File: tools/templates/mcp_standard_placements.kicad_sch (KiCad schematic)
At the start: 150 parts, among them J1 ICSP, J3 PIR BOARD, J5 MOTOR, J6 DNP, Q1 FMOS3401A?, Q11 MMBTA55?, Q2 BC847B?, Q3 MMBTA55?, Q4 MMBTA55?, Q5 MMBTA55?, Q6 MMBTA55?, Q7 BC857C?, Q8 N/P pair? (372A), Q9 DNP, U1 S-1200B45? [pins], U106 U6A / DNP, U2 SN74LVC2G14DBV?, U3 SGM8542XS, U4 PIC16F18855, U5 MX512H, U6 S-812C33AMC? / 3.3V, U7 DNP, Y1 20 MHz

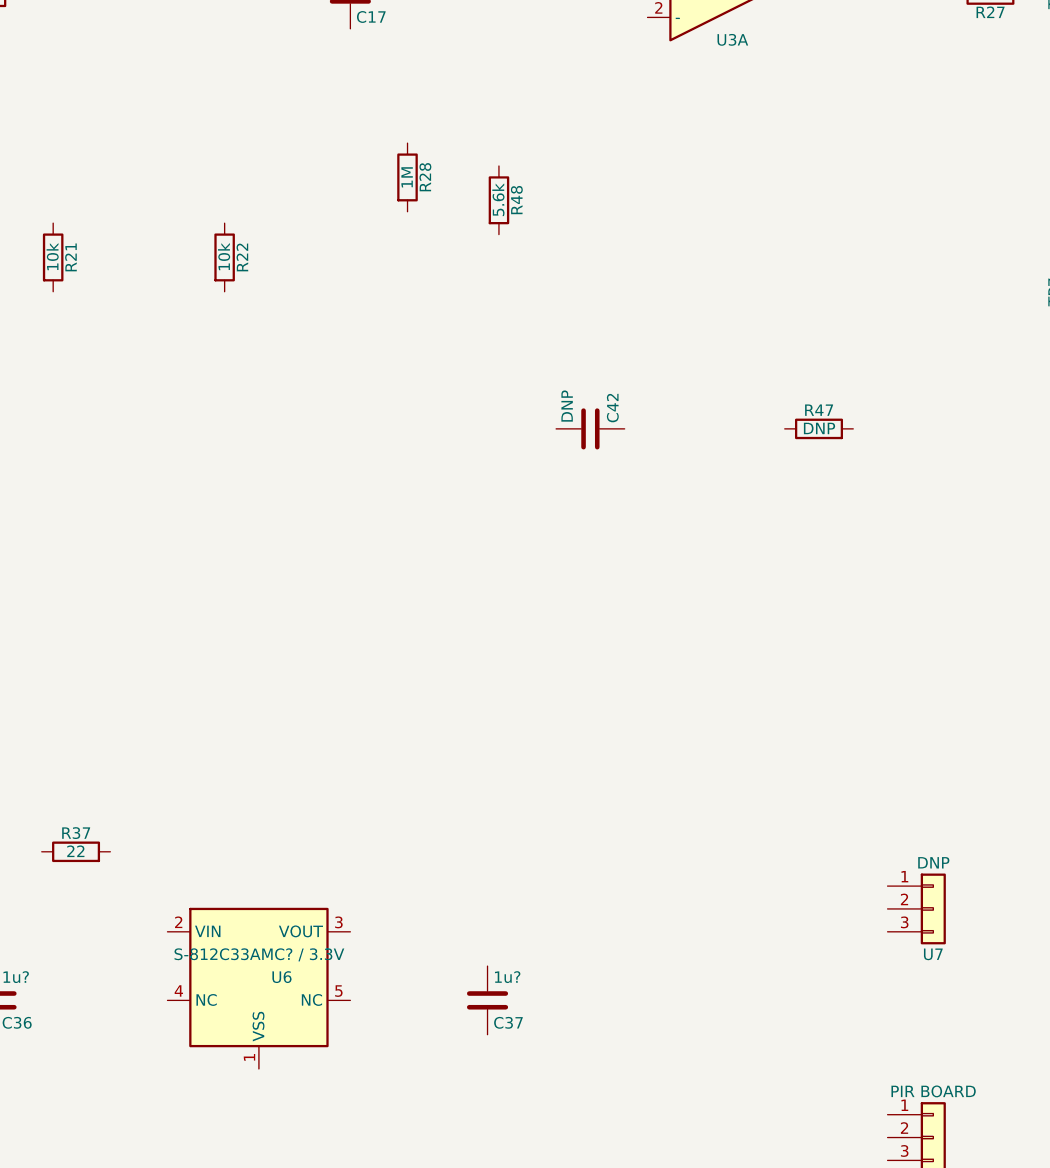
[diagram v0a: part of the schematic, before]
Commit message: Resolve receiver option wiring and measured D6 U6 connections
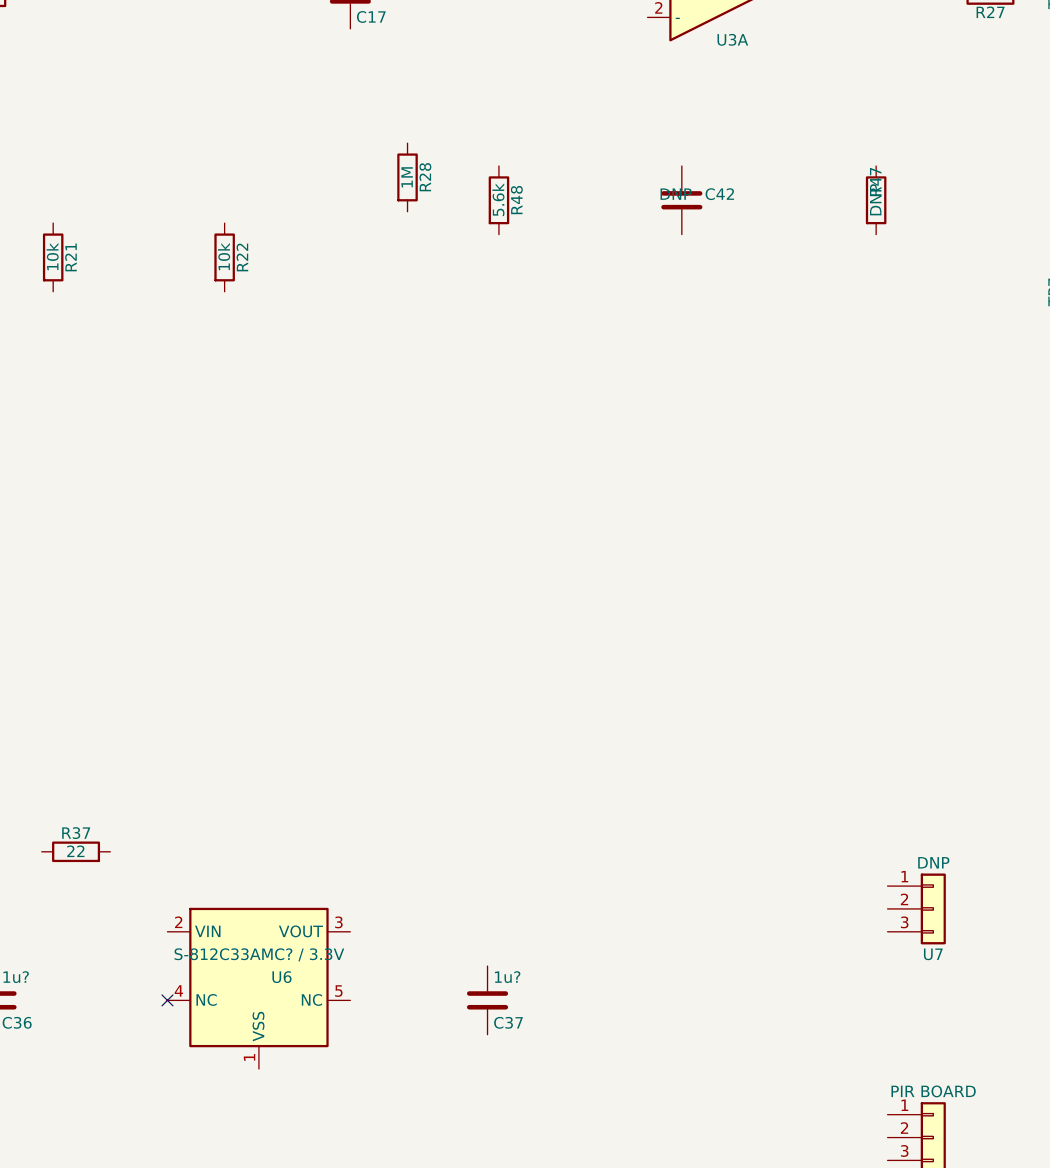
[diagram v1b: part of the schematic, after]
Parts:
- C42, R25, R47, R48: ConnectionEvidence (none) -> v0.9.19 user annotated local copper: R47 left -> U3.1/R27 r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
- D6: ConnectionEvidence (none) -> v0.9.20 B22-B27: upper photo contact V -> GND, lower W -> V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
- U6: ConnectionEvidence (none) -> v0.9.20: U6.5-U6.2 measured 1 ohm (B28). User annotation al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
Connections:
- no-connect marks 0 -> 1
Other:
- moved on the sheet: C42, R47
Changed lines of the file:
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@@
 			)
 		)
-    (property "ConnectionEvidence" "v0.9.18: C6 is reconstructed in parallel with C5 from the user proposal and photos IMG_2431/IMG_2432. C6 upper pad/model1 joins the C5-positive supply copper (H_RF_VDD, after L1); lower pad/model2 joins GND. Photo-supported, not a new meter-confirmed connection. C6 capacitance remains unknown. Earlier 400 kohm output exclusion and 10 ohm Q8-supply-path reading are retained; the latter does not independently prove Q8 source wiring." (at 237.49 181.61 0)
-      (effects (font (size 1.27 1.27)) (hide yes))
-    )
+		(property "ConnectionEvidence" "v0.9.18: C6 is reconstructed in parallel with C5 from the user proposal and photos IMG_2431/IMG_2432. C6 upper pad/model1 joins the C5-positive supply copper (H_RF_VDD, after L1); lower pad/model2 joins GND. Photo-supported, not a new meter-confirmed connection. C6 capacitance remains unknown. Earlier 400 kohm output exclusion and 10 ohm Q8-supply-path reading are retained; the latter does not independently prove Q8 source wiring."
+			(at 237.49 181.61 0)
+			(effects
+				(font
+					(size 1.27 1.27)
+				)
+				(hide yes)
+			)
+		)
 		(pin "1"
 		)
@@
 			)
 		)
-    (property "ConnectionEvidence" "v0.9.18: C6 is reconstructed in parallel with C5 from the user proposal and photos IMG_2431/IMG_2432. C6 upper pad/model1 joins the C5-positive supply copper (H_RF_VDD, after L1); lower pad/model2 joins GND. Photo-supported, not a new meter-confirmed connection. C6 capacitance remains unknown. Earlier 400 kohm output exclusion and 10 ohm Q8-supply-path reading are retained; the latter does not independently prove Q8 source wiring." (at 259.08 181.61 0)
-      (effects (font (size 1.27 1.27)) (hide yes))
-    )
+		(property "ConnectionEvidence" "v0.9.18: C6 is reconstructed in parallel with C5 from the user proposal and photos IMG_2431/IMG_2432. C6 upper pad/model1 joins the C5-positive supply copper (H_RF_VDD, after L1); lower pad/model2 joins GND. Photo-supported, not a new meter-confirmed connection. C6 capacitance remains unknown. Earlier 400 kohm output exclusion and 10 ohm Q8-supply-path reading are retained; the latter does not independently prove Q8 source wiring."
+			(at 259.08 181.61 0)
+			(effects
+				(font
+					(size 1.27 1.27)
+				)
+				(hide yes)
+			)
+		)
 		(pin "1"
 		)
@@
 			)
 		)
+		(property "ConnectionEvidence" "v0.9.19 user annotated local copper: R47 left -> U3.1/R27 right; R47 right + C42 lower + R25 lower + R48 right share RX_STAGE_LINK. C42 upper -> GND inferred from continuous copper beside U3.4 in IMG_2429/2434. R25-GND and R48-VREF old assumptions withdrawn. R47/C42 remain DNP. No meter reading supplied."
+			(at 356.87 223.52 0)
+			(effects
+				(font
+					(size 1.27 1.27)
+				)
+				(hide yes)
+			)
+		)
 		(pin "1"
 		)
@@
 			)
 		)
+		(property "ConnectionEvidence" "v0.9.19 user annotated local copper: R47 left -> U3.1/R27 right; R47 right + C42 lower + R25 lower + R48 right share RX_STAGE_LINK. C42 upper -> GND inferred from continuous copper beside U3.4 in IMG_2429/2434. R25-GND and R48-VREF old assumptions withdrawn. R47/C42 remain DNP. No meter reading supplied."
+			(at 527.05 215.9 0)
+			(effects
+				(font
+					(size 1.27 1.27)
+				)
+				(hide yes)
+			)
+		)
 		(pin "1"
 		)
@@
 	(symbol
 		(lib_id "Device:C")
-		(at 367.03 248.92 90)
+		(at 377.19 223.52 0)
 		(unit 1)
 		(body_style 1)
@@
 		(dnp no)
 		(property "Reference" "C42"
-			(at 369.57 248.285 0)
+			(at 379.73 222.88500000000002 0)
 			(show_name no)
 			(do_not_autoplace no)
@@
 		)
 		(property "Value" "DNP"
-			(at 364.49 248.285 0)
+			(at 374.65000000000003 222.88500000000002 0)
 			(show_name no)
 			(do_not_autoplace no)
@@
 		)
 		(property "Footprint" "Capacitor_SMD:C_0603_1608Metric"
-			(at 363.22 247.955 0)
+			(at 373.38000000000005 222.55500000000004 0)
 			(hide yes)
 			(show_name no)
@@
 		)
 		(property "Datasheet" ""
-			(at 367.03 248.92 0)
+			(at 377.19 223.52 0)
 			(hide yes)
 			(show_name no)
@@
 		)
 		(property "Description" "Unpolarized capacitor"
-			(at 367.03 248.92 0)
+			(at 377.19 223.52 0)
 			(hide yes)
 			(show_name no)
@@
 			)
 		)
+		(property "ConnectionEvidence" "v0.9.19 user annotated local copper: R47 left -> U3.1/R27 right; R47 right + C42 lower + R25 lower + R48 right share RX_STAGE_LINK. C42 upper -> GND inferred from continuous copper beside U3.4 in IMG_2429/2434. R25-GND and R48-VREF old assumptions withdrawn. R47/C42 remain DNP. No meter reading supplied."
+			(at 377.19 223.52 0)
+			(effects
+				(font
+					(size 1.27 1.27)
+				)
+				(hide yes)
+			)
+		)
 		(pin "1"
 		)
@@
 	(symbol
 		(lib_id "Device:R")
-		(at 392.43 248.92 90)
+		(at 398.78 223.52 0)
 		(unit 1)
 		(body_style 1)
@@
 		(dnp no)
 		(property "Reference" "R47"
-			(at 392.43 246.888 90)
+			(at 398.78 221.48800000000003 90)
 			(show_name no)
 			(do_not_autoplace no)
@@
 		)
 		(property "Value" "DNP"
-			(at 392.43 248.92 90)
+			(at 398.78 223.52 90)
 			(show_name no)
 			(do_not_autoplace no)
@@
 		)
 		(property "Footprint" "Resistor_SMD:R_0603_1608Metric"
-			(at 392.43 250.698 90)
+			(at 398.78 225.29800000000003 90)
 			(hide yes)
 			(show_name no)
@@
 		)
 		(property "Datasheet" ""
-			(at 392.43 248.92 0)
+			(at 398.78 223.52 0)
 			(hide yes)
 			(show_name no)
@@
 		)
 		(property "Description" "Resistor"
-			(at 392.43 248.92 0)
+			(at 398.78 223.52 0)
 			(hide yes)
 			(show_name no)
@@
 			)
 		)
+		(property "ConnectionEvidence" "v0.9.19 user annotated local copper: R47 left -> U3.1/R27 right; R47 right + C42 lower + R25 lower + R48 right share RX_STAGE_LINK. C42 upper -> GND inferred from continuous copper beside U3.4 in IMG_2429/2434. R25-GND and R48-VREF old assumptions withdrawn. R47/C42 remain DNP. No meter reading supplied."
+			(at 398.78 223.52 0)
+			(effects
+				(font
+					(size 1.27 1.27)
+				)
+				(hide yes)
+			)
+		)
 		(pin "1"
 		)
@@
 		)
 	)
+	(no_connect
+		(at 320.03999999999996 312.42)
+	)
 	(sheet_instances
 		(path "/"
@@
 			)
 		)
+		(property "ConnectionEvidence" "v0.9.20: U6.5-U6.2 measured 1 ohm (B28). User annotation also joins physical L2/native5 to R37 upper/model2 and empty U6A single/native1. U6.4/L1 marked NC by user and appears as an isolated surface stub in original photos. Candidate pin5 is internally NC but externally tied to VIN; pin4 remains unused."
+			(at 330.2 309.88 0)
+			(effects
+				(font
+					(size 1.27 1.27)
+				)
+				(hide yes)
+			)
+		)
 		(pin "1"
 		)
@@
 			)
 		)
+    (property "ConnectionEvidence" "v0.9.20 B22-B27: upper photo contact V -> GND, lower W -> VPP, each 1 ohm. B29 red V/black W about 0.7V; B30 reverse OL. Supports A=V/GND (pin2), K=W/VPP (pin1). G3 identity and Zener breakdown remain unverified; no 3.9V measurement." (at 405.13 391.16 0)
+      (effects (font (size 1.27 1.27)) (hide yes))
+    )
 		(pin "1"
 		)

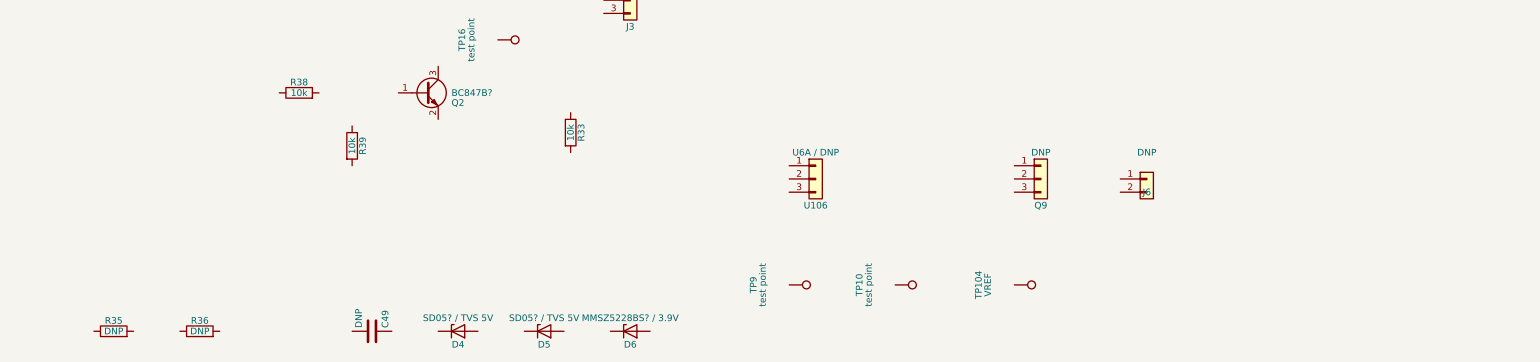
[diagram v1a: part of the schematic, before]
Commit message: Map J6 Q9 option and correct button routing to VPP
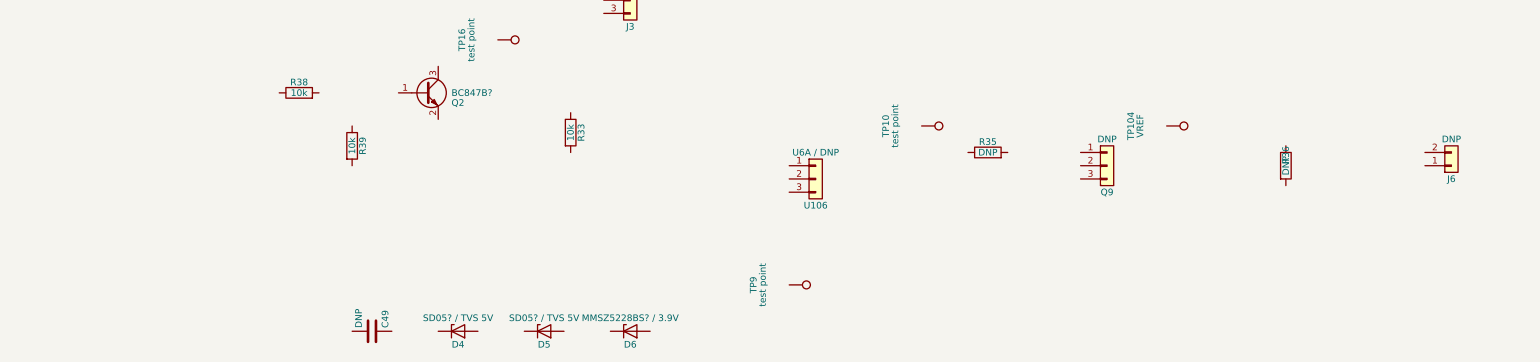
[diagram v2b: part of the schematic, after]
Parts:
- C35, R40, R41, S1: ConnectionEvidence (none) -> v0.9.21 user annotated S1 upper-right to C35 upper/model2 (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
- J6, Q9, R35, R36, TP10: ConnectionEvidence (none) -> v0.9.21 annotated photo: J6 left/model1 joins Q9 single/nat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
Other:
- moved on the sheet: J6, Q9, R35, R36, TP10, TP104

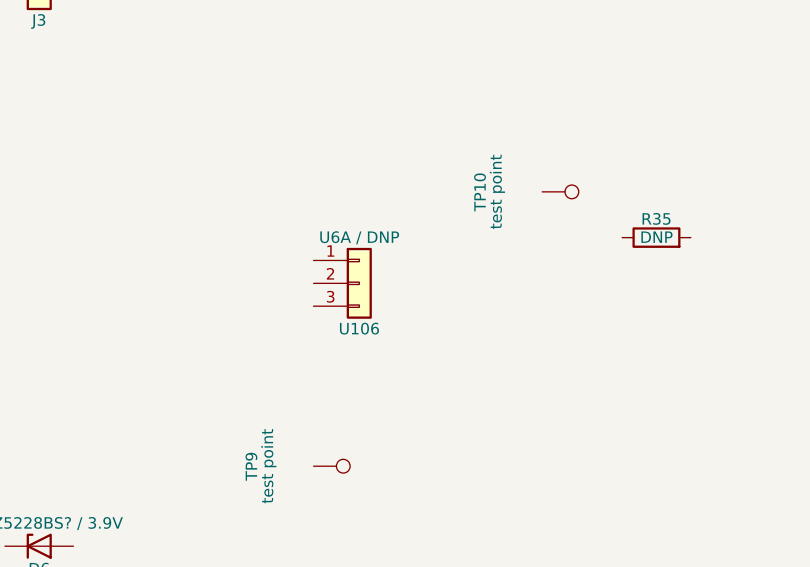
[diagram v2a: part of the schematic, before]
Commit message: Complete U6A option pad mapping with confirmed ground
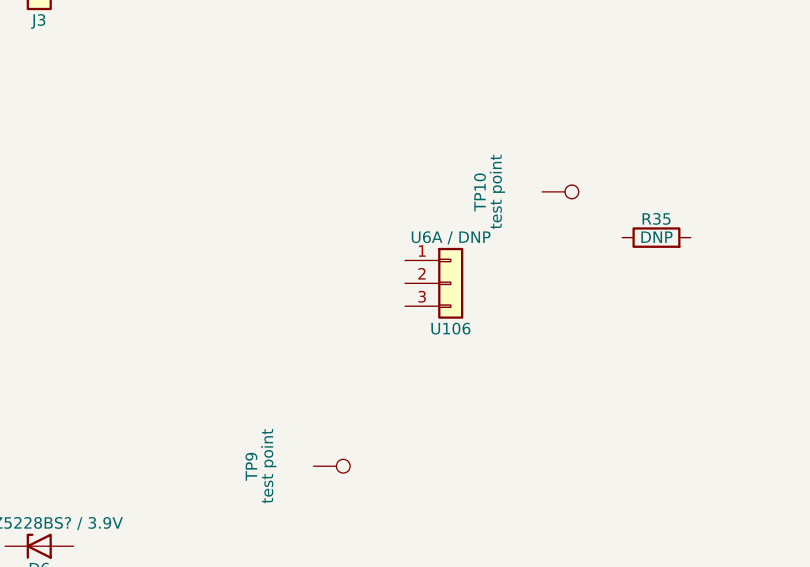
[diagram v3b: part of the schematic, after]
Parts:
- U106: ConnectionEvidence (none) -> v0.9.22 user annotated U6A option: single left pad/model L/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
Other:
- moved on the sheet: U106
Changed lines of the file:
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@@
 	(symbol
 		(lib_id "Connector_Generic:Conn_01x03")
-		(at 440.69 361.95 0)
+		(at 450.85 361.95 0)
 		(unit 1)
 		(body_style 1)
@@
 		(dnp no)
 		(property "Reference" "U106"
-			(at 440.69 367.03 0)
+			(at 450.85 367.03 0)
 			(show_name no)
 			(do_not_autoplace no)
@@
 		)
 		(property "Value" "U6A / DNP"
-			(at 440.69 356.87 0)
+			(at 450.85 356.87 0)
 			(show_name no)
 			(do_not_autoplace no)
@@
 		)
 		(property "Footprint" "Package_TO_SOT_SMD:SOT-23"
-			(at 440.69 361.95 0)
+			(at 450.85 361.95 0)
 			(hide yes)
 			(show_name no)
@@
 		)
 		(property "Datasheet" ""
-			(at 440.69 361.95 0)
+			(at 450.85 361.95 0)
 			(hide yes)
 			(show_name no)
@@
 		)
 		(property "Description" "Generic connector, single row, 01x03, script generated (kicad-library-utils/schlib/autogen/connector/)"
-			(at 440.69 361.95 0)
+			(at 450.85 361.95 0)
 			(hide yes)
 			(show_name no)
@@
 		)
 		(property "ViaEvidence" "v0.9.8: User confirms V067-J3 pin1 (red wire), on modeled H_PIR_VDD. Prior V067-U6A.R1 local pad association retained. Empty U6A option remains DNP; this does not identify an IC or confirm every other H_PIR_VDD branch."
-			(at 440.69 361.95 0)
+			(at 450.85 361.95 0)
 			(effects
 				(font
+					(size 1.27 1.27)
+				)
+				(hide yes)
+			)
+		)
+		(property "ConnectionEvidence" "v0.9.22 user annotated U6A option: single left pad/model L/native U106.1 joins U6 pin5 and the existing input node after R37; upper-right/model R1/native2 joins J3.1 (red PIR wire); lower-right/model R2/native3 joins GND. All three external pads mapped, option remains DNP. User called the input VDD; retain VDD -> R37 (22 ohm) -> H_AUX_IN because the annotation ends at U6 pin5 and prior B28 confirms pin5-pin2, not a bypass across R37. No fitted IC identity or voltage measurement implied."
+			(at 450.85 361.95 0)
+			(effects
+				(font
